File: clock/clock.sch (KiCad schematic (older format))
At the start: 2 parts

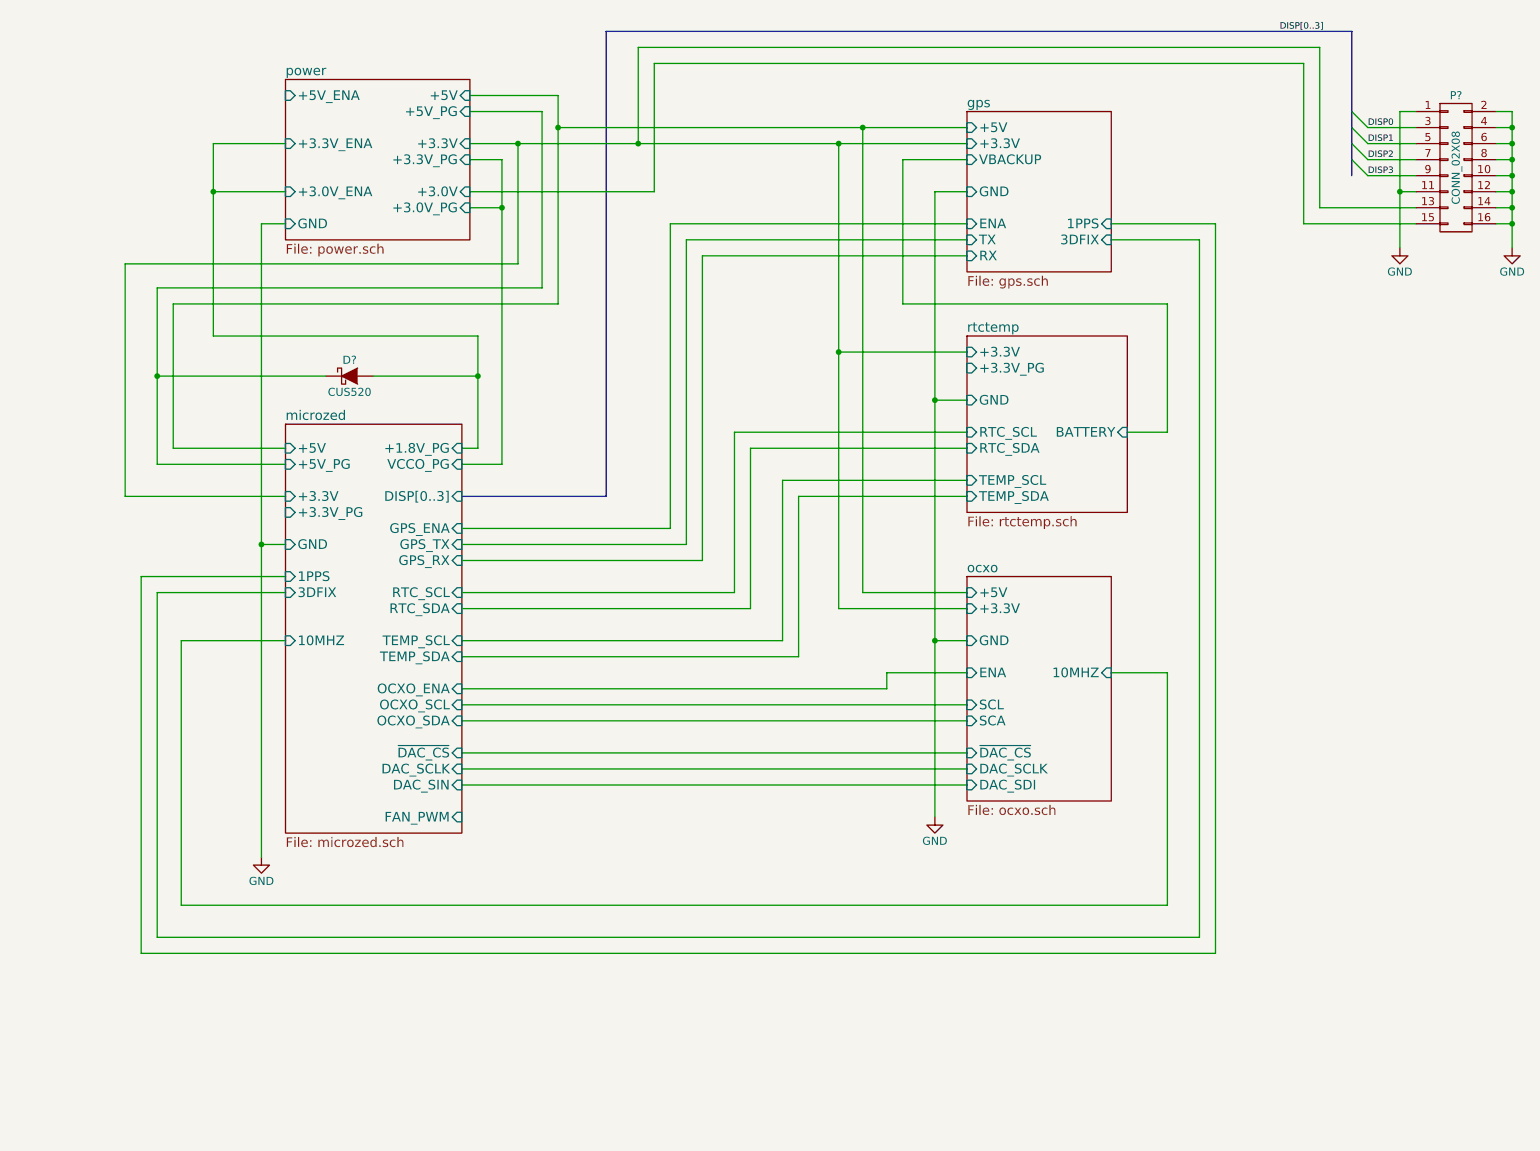
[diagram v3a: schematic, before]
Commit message: Add proper loading and buffer to the OCXO output.
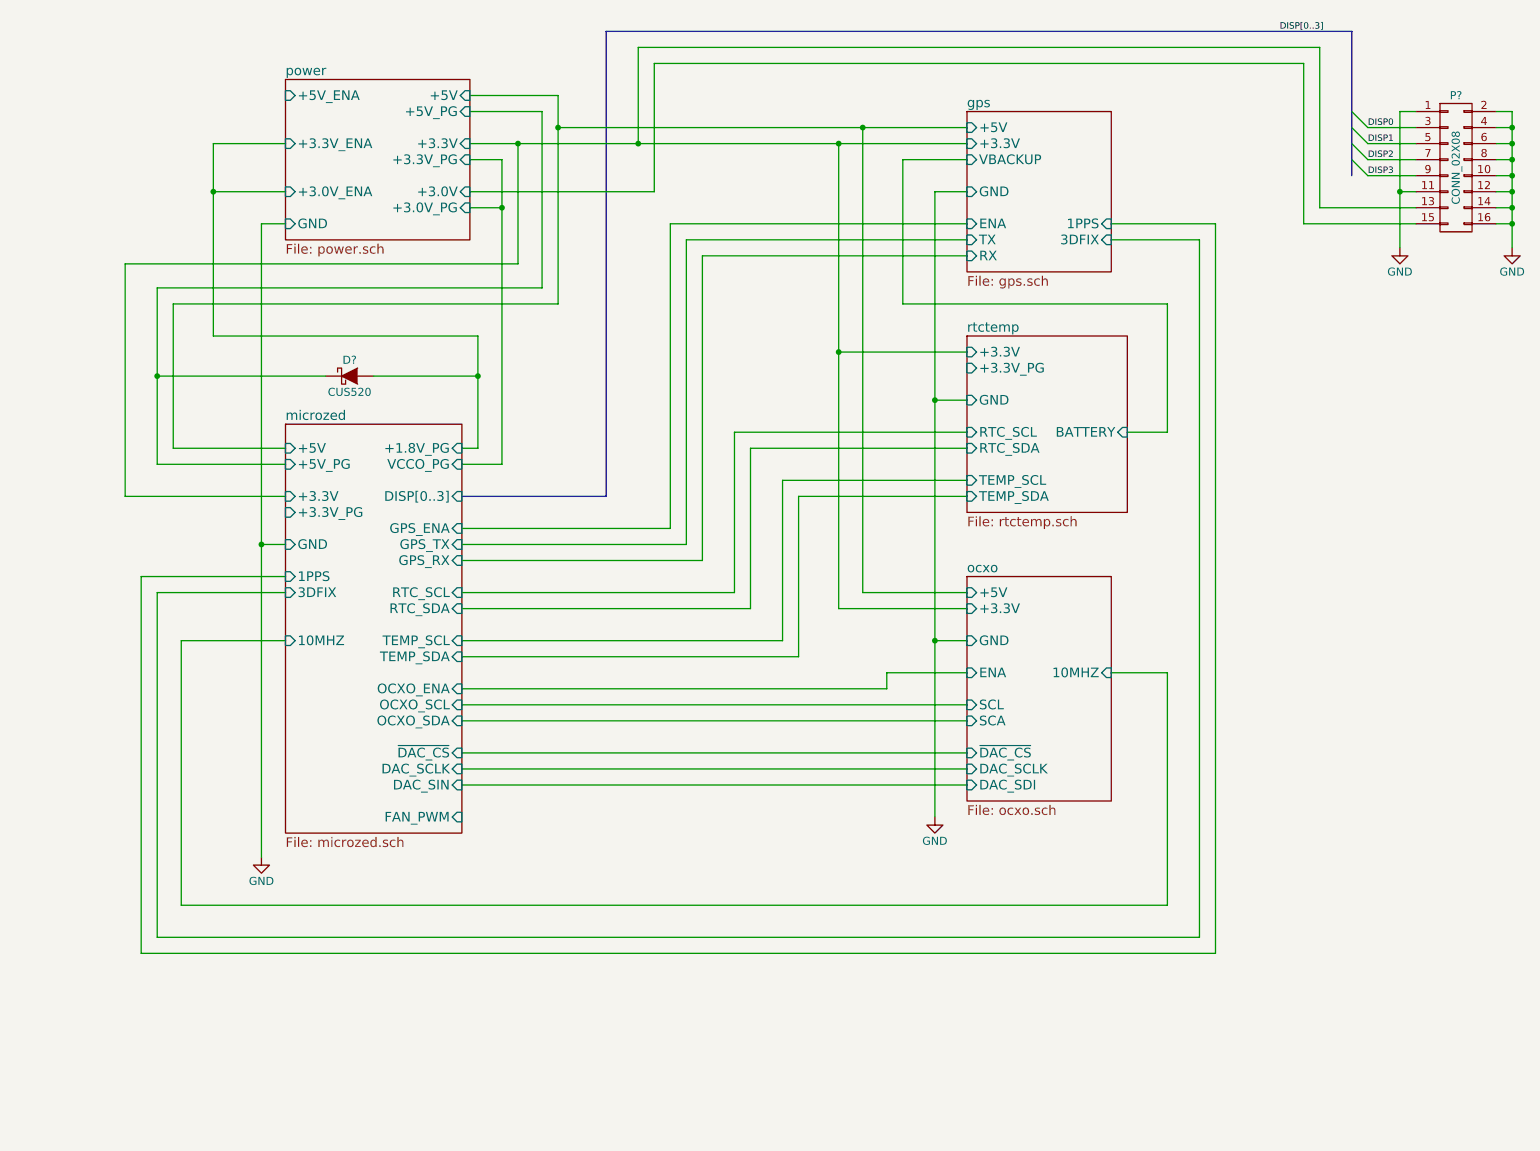
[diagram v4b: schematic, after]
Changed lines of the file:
@@
 	3550 1000 4100 1000
 Wire Wire Line
-	4100 1000 4100 1200
-Wire Wire Line
-	4100 1200 4100 2300
+	4100 1000 4100 2300
 Wire Wire Line
 	4100 2300 1700 2300
@@
 	4000 1100 4000 2200
 Wire Wire Line
-	1950 1300 1950 1600
-Wire Wire Line
-	1950 1600 1950 2500
+	1950 1300 1950 2500
 Wire Wire Line
 	1950 1300 2400 1300
@@
 	1750 4400 2400 4400
 Wire Wire Line
-	4100 1200 6000 1200
-Wire Wire Line
-	6000 1200 6650 1200
-Wire Wire Line
-	3550 1300 3850 1300
-Wire Wire Line
-	3850 1300 4600 1300
-Wire Wire Line
-	4600 1300 5850 1300
-Wire Wire Line
-	5850 1300 6650 1300
+	4100 1200 6650 1200
+Wire Wire Line
+	3550 1300 6650 1300
 Wire Wire Line
 	6000 1200 6000 4100
@@
 	5850 4200 6650 4200
 Wire Wire Line
-	5850 1300 5850 2600
-Wire Wire Line
-	5850 2600 5850 4200
+	5850 1300 5850 4200
 Connection ~ 5850 1300
 Wire Wire Line
@@
 	2400 3800 2250 3800
 Wire Wire Line
-	2250 1800 2250 3800
-Wire Wire Line
-	2250 3800 2250 5750
+	2250 1800 2250 5750
 Wire Wire Line
 	6650 1600 6450 1600
 Wire Wire Line
-	6450 1600 6450 2900
-Wire Wire Line
-	6450 2900 6450 4400
-Wire Wire Line
-	6450 4400 6450 5500
+	6450 1600 6450 5500
 Wire Wire Line
 	2400 1800 2250 1800
@@
 	3550 1400 3750 1400
 Wire Wire Line
-	3750 1400 3750 1700
-Wire Wire Line
-	3750 1700 3750 3300
+	3750 1400 3750 3300
 Wire Wire Line
 	3750 3300 3500 3300
@@
 	3600 3200 3500 3200
 Wire Wire Line
-	3600 2500 3600 2750
-Wire Wire Line
-	3600 2750 3600 3200
+	3600 2500 3600 3200
 Wire Wire Line
 	1950 2500 3600 2500
@@
 	4000 2200 1600 2200
 Wire Wire Line
-	1600 2200 1600 2750
-Wire Wire Line
-	1600 2750 1600 3300
+	1600 2200 1600 3300
 Wire Wire Line
 	1600 3300 2400 3300
@@
 	9950 1100 10050 1100
 Wire Wire Line
-	10050 1100 10050 1200
-Wire Wire Line
-	10050 1200 10050 1300
-Wire Wire Line
-	10050 1300 10050 1400
-Wire Wire Line
-	10050 1400 10050 1500
-Wire Wire Line
-	10050 1500 10050 1600
-Wire Wire Line
-	10050 1600 10050 1700
-Wire Wire Line
-	10050 1700 10050 1800
-Wire Wire Line
-	10050 1800 10050 1950
+	10050 1100 10050 1950
 Wire Wire Line
 	9950 1800 10050 1800
@@
 	9450 1100 9350 1100
 Wire Wire Line
-	9350 1100 9350 1600
-Wire Wire Line
-	9350 1600 9350 1950
+	9350 1100 9350 1950
 Wire Wire Line
 	9450 1600 9350 1600
@@
 	4400 600  9050 600
 Wire Bus Line
-	9050 600  9050 1100
-Wire Bus Line
-	9050 1100 9050 1200
-Wire Bus Line
-	9050 1200 9050 1300
-Wire Bus Line
-	9050 1300 9050 1400
-Wire Bus Line
-	9050 1400 9050 1500
+	9050 600  9050 1500
 Entry Wire Line
 	9050 1100 9150 1200

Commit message: Fan and power connectors.
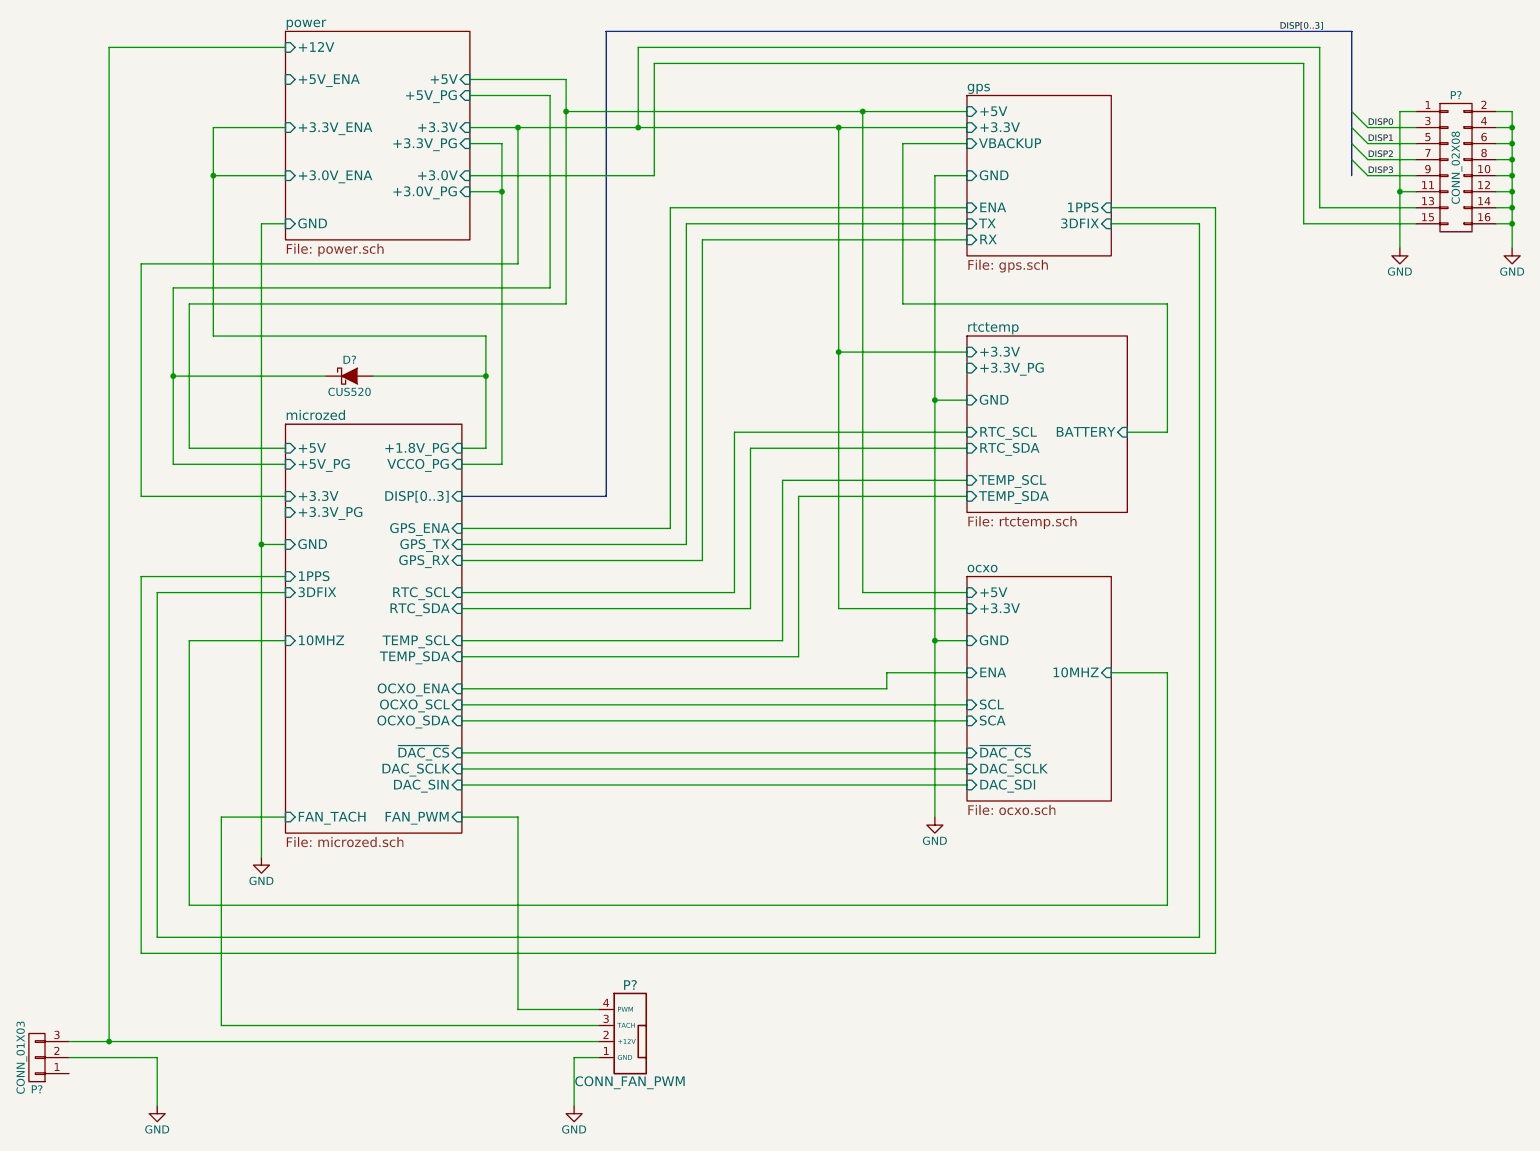
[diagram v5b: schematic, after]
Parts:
- added P?: CONN_01X03, symbol CONN_01X03
- added P?: CONN_FAN_PWM, symbol CONN_FAN_PWM
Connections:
- net GND: now also P?.1 (GND), P?.2 (P2)
- net microzed/FAN_PWM: now also P?.4 (PWM)
- new net microzed/FAN_TACH: P?.3 (TACH)
- new net power/+12V: P?.2 (+12V), P?.3 (P3)
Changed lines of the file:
@@
 $EndSheet
 $Sheet
-S 6650 1100 900  1000
+S 6650 1000 900  1000
 U 56133D72
 F0 "gps" 60
 F1 "gps.sch" 60
-F2 "+5V" I L 6650 1200 60
-F3 "+3.3V" I L 6650 1300 60
-F4 "TX" I L 6650 1900 60
-F5 "RX" I L 6650 2000 60
-F6 "1PPS" I R 7550 1800 60
-F7 "3DFIX" I R 7550 1900 60
-F8 "VBACKUP" I L 6650 1400 60
-F9 "GND" I L 6650 1600 60
-F10 "ENA" I L 6650 1800 60
+F2 "+5V" I L 6650 1100 60
+F3 "+3.3V" I L 6650 1200 60
+F4 "TX" I L 6650 1800 60
+F5 "RX" I L 6650 1900 60
+F6 "1PPS" I R 7550 1700 60
+F7 "3DFIX" I R 7550 1800 60
+F8 "VBACKUP" I L 6650 1300 60
+F9 "GND" I L 6650 1500 60
+F10 "ENA" I L 6650 1700 60
 $EndSheet
 $Sheet
@@
 F25 "TEMP_SCL" I R 3500 4400 60
 F26 "TEMP_SDA" I R 3500 4500 60
+F27 "FAN_TACH" I L 2400 5500 60
 $EndSheet
 Wire Wire Line
-	3550 1000 4100 1000
-Wire Wire Line
-	4100 1000 4100 2300
-Wire Wire Line
-	4100 2300 1700 2300
-Wire Wire Line
-	1700 2300 1700 3200
-Wire Wire Line
-	1700 3200 2400 3200
-Wire Wire Line
-	3550 1100 4000 1100
-Wire Wire Line
-	4000 1100 4000 2200
-Wire Wire Line
-	1950 1300 1950 2500
-Wire Wire Line
-	1950 1300 2400 1300
-Wire Wire Line
-	2400 1600 1950 1600
-Connection ~ 1950 1600
+	3550 900  4150 900
+Wire Wire Line
+	4150 900  4150 2300
+Wire Wire Line
+	4150 2300 1800 2300
+Wire Wire Line
+	1800 2300 1800 3200
+Wire Wire Line
+	1800 3200 2400 3200
+Wire Wire Line
+	3550 1000 4050 1000
+Wire Wire Line
+	4050 1000 4050 2200
+Wire Wire Line
+	1950 1200 1950 2500
+Wire Wire Line
+	1950 1200 2400 1200
+Wire Wire Line
+	2400 1500 1950 1500
+Connection ~ 1950 1500
 Wire Wire Line
 	7550 4600 7900 4600
@@
 	7900 4600 7900 6050
 Wire Wire Line
-	7900 6050 1750 6050
-Wire Wire Line
-	1750 6050 1750 4400
-Wire Wire Line
-	1750 4400 2400 4400
-Wire Wire Line
-	4100 1200 6650 1200
-Wire Wire Line
-	3550 1300 6650 1300
-Wire Wire Line
-	6000 1200 6000 4100
+	7900 6050 1800 6050
+Wire Wire Line
+	1800 6050 1800 4400
+Wire Wire Line
+	1800 4400 2400 4400
+Wire Wire Line
+	4150 1100 6650 1100
+Wire Wire Line
+	3550 1200 6650 1200
+Wire Wire Line
+	6000 1100 6000 4100
 Wire Wire Line
 	6000 4100 6650 4100
-Connection ~ 6000 1200
+Connection ~ 6000 1100
 Wire Wire Line
 	5850 4200 6650 4200
 Wire Wire Line
-	5850 1300 5850 4200
-Connection ~ 5850 1300
+	5850 1200 5850 4200
+Connection ~ 5850 1200
 Wire Wire Line
 	6150 4700 3500 4700
@@
 	3500 3700 4800 3700
 Wire Wire Line
-	4800 3700 4800 1800
-Wire Wire Line
-	4800 1800 6650 1800
-Wire Wire Line
-	6650 1900 4900 1900
-Wire Wire Line
-	4900 1900 4900 3800
+	4800 3700 4800 1700
+Wire Wire Line
+	4800 1700 6650 1700
+Wire Wire Line
+	6650 1800 4900 1800
+Wire Wire Line
+	4900 1800 4900 3800
 Wire Wire Line
 	4900 3800 3500 3800
@@
 	3500 3900 5000 3900
 Wire Wire Line
-	5000 3900 5000 2000
-Wire Wire Line
-	5000 2000 6650 2000
-Wire Wire Line
-	7550 1900 8100 1900
-Wire Wire Line
-	8100 1900 8100 6250
+	5000 3900 5000 1900
+Wire Wire Line
+	5000 1900 6650 1900
+Wire Wire Line
+	7550 1800 8100 1800
+Wire Wire Line
+	8100 1800 8100 6250
 Wire Wire Line
 	8100 6250 1600 6250
@@
 	1500 6350 8200 6350
 Wire Wire Line
-	8200 6350 8200 1800
-Wire Wire Line
-	8200 1800 7550 1800
-Wire Wire Line
-	3850 1300 3850 2050
-Wire Wire Line
-	3850 2050 1400 2050
-Wire Wire Line
-	1400 2050 1400 3500
-Wire Wire Line
-	1400 3500 2400 3500
-Connection ~ 3850 1300
+	8200 6350 8200 1700
+Wire Wire Line
+	8200 1700 7550 1700
+Wire Wire Line
+	3850 1200 3850 2050
+Wire Wire Line
+	3850 2050 1500 2050
+Wire Wire Line
+	1500 2050 1500 3500
+Wire Wire Line
+	1500 3500 2400 3500
+Connection ~ 3850 1200
 Wire Wire Line
 	2400 3800 2250 3800
@@
 	2250 1800 2250 5750
 Wire Wire Line
-	6650 1600 6450 1600
-Wire Wire Line
-	6450 1600 6450 5500
+	6650 1500 6450 1500
+Wire Wire Line
+	6450 1500 6450 5500
 Wire Wire Line
 	2400 1800 2250 1800
@@
 $EndComp
 Wire Wire Line
-	3550 1400 3750 1400
-Wire Wire Line
-	3750 1400 3750 3300
+	3550 1300 3750 1300
+Wire Wire Line
+	3750 1300 3750 3300
 Wire Wire Line
 	3750 3300 3500 3300
 Wire Wire Line
-	3750 1700 3550 1700
-Connection ~ 3750 1700
-Wire Wire Line
-	3600 3200 3500 3200
-Wire Wire Line
-	3600 2500 3600 3200
-Wire Wire Line
-	1950 2500 3600 2500
-Wire Wire Line
-	4000 2200 1600 2200
-Wire Wire Line
-	1600 2200 1600 3300
-Wire Wire Line
-	1600 3300 2400 3300
+	3750 1600 3550 1600
+Connection ~ 3750 1600
+Wire Wire Line
+	3650 3200 3500 3200
+Wire Wire Line
+	3650 2500 3650 3200
+Wire Wire Line
+	1950 2500 3650 2500
+Wire Wire Line
+	4050 2200 1700 2200
+Wire Wire Line
+	1700 2200 1700 3300
+Wire Wire Line
+	1700 3300 2400 3300
 $Comp
 L D_Schottky D?
@@
 $EndComp
 Wire Wire Line
-	3600 2750 2950 2750
-Connection ~ 3600 2750
-Wire Wire Line
-	2650 2750 1600 2750
-Connection ~ 1600 2750
+	3650 2750 2950 2750
+Connection ~ 3650 2750
+Wire Wire Line
+	2650 2750 1700 2750
+Connection ~ 1700 2750
 $Sheet
-S 2400 900  1150 1000
+S 2400 600  1150 1300
 U 55FF5A67
 F0 "power" 60
 F1 "power.sch" 60
-F2 "+5V" I R 3550 1000 60
-F3 "+3.3V" I R 3550 1300 60
-F4 "+3.0V" I R 3550 1600 60
-F5 "+3.0V_PG" I R 3550 1700 60
-F6 "+3.3V_PG" I R 3550 1400 60
-F7 "+5V_PG" I R 3550 1100 60
-F8 "+5V_ENA" I L 2400 1000 60
-F9 "+3.3V_ENA" I L 2400 1300 60
-F10 "+3.0V_ENA" I L 2400 1600 60
+F2 "+5V" I R 3550 900 60
+F3 "+3.3V" I R 3550 1200 60
+F4 "+3.0V" I R 3550 1500 60
+F5 "+3.0V_PG" I R 3550 1600 60
+F6 "+3.3V_PG" I R 3550 1300 60
+F7 "+5V_PG" I R 3550 1000 60
+F8 "+5V_ENA" I L 2400 900 60
+F9 "+3.3V_ENA" I L 2400 1200 60
+F10 "+3.0V_ENA" I L 2400 1500 60
 F11 "GND" I L 2400 1800 60
+F12 "+12V" I L 2400 700 60
 $EndSheet
 $Comp
@@
 Connection ~ 9350 1600
 Wire Wire Line
-	3550 1600 4700 1600
-Wire Wire Line
-	4700 1600 4700 800
+	3550 1500 4700 1500
+Wire Wire Line
+	4700 1500 4700 800
 Wire Wire Line
 	4700 800  8750 800
@@
 	8850 700  4600 700
 Wire Wire Line
-	4600 700  4600 1300
-Connection ~ 4600 1300
+	4600 700  4600 1200
+Connection ~ 4600 1200
 $Sheet
 S 6650 2500 1000 1100
@@
 	7900 2300 6250 2300
 Wire Wire Line
-	6250 2300 6250 1400
-Wire Wire Line
-	6250 1400 6650 1400
+	6250 2300 6250 1300
+Wire Wire Line
+	6250 1300 6650 1300
 Wire Bus Line
 	3500 3500 4400 3500
@@
 Wire Wire Line
 	6150 4600 6150 4700
-Connection ~ 4100 1200
+Connection ~ 4150 1100
+$Comp
+L CONN_FAN_PWM P?
+U 1 1 563D6A73
+P 4550 6850
+F 0 "P?" H 4550 7150 60  0000 C CNN
+F 1 "CONN_FAN_PWM" H 4550 6550 60  0000 C CNN
+F 2 "" H 4750 6800 60  0000 C CNN
+F 3 "" H 4750 6800 60  0000 C CNN
+F 4 "Molex" H 4550 7350 50  0001 C CNN "Manufacturer"
+F 5 "47053-1000" H 4550 7250 50  0001 C CNN "PartNum"
+	1    4550 6850
+	1    0    0    -1
+$EndComp
+Wire Wire Line
+	3500 5500 3850 5500
+Wire Wire Line
+	3850 5500 3850 6700
+Wire Wire Line
+	3850 6700 4350 6700
+Wire Wire Line
+	2000 6800 4350 6800
+Wire Wire Line
+	2000 6800 2000 5500
+Wire Wire Line
+	2000 5500 2400 5500
+$Comp
+L GND #PWR?
+U 1 1 563D71E9
+P 4200 7300
+F 0 "#PWR?" H 4200 7050 50  0001 C CNN
+F 1 "GND" H 4200 7150 50  0000 C CNN
+F 2 "" H 4200 7300 60  0000 C CNN
+F 3 "" H 4200 7300 60  0000 C CNN
+	1    4200 7300
+	1    0    0    -1
+$EndComp
+Wire Wire Line
+	4350 7000 4200 7000
+Wire Wire Line
+	4200 7000 4200 7300
+Wire Wire Line
+	2400 700  1300 700
+Wire Wire Line
+	1300 700  1300 6900
+Wire Wire Line
+	1050 6900 4350 6900
+$Comp
+L CONN_01X03 P?
+U 1 1 563D5B9B
+P 850 7000
+F 0 "P?" H 850 7200 50  0000 C CNN
+F 1 "CONN_01X03" V 950 7000 50  0000 C CNN
+F 2 "" H 850 7000 60  0000 C CNN
+F 3 "" H 850 7000 60  0000 C CNN
+	1    850  7000
+	-1   0    0    1
+$EndComp
+Connection ~ 1300 6900
+Wire Wire Line
+	1050 7000 1600 7000
+Wire Wire Line
+	1600 7000 1600 7300
+$Comp
+L GND #PWR?
+U 1 1 563D694B
+P 1600 7300
+F 0 "#PWR?" H 1600 7050 50  0001 C CNN
+F 1 "GND" H 1600 7150 50  0000 C CNN
+F 2 "" H 1600 7300 60  0000 C CNN
+F 3 "" H 1600 7300 60  0000 C CNN
+	1    1600 7300
+	1    0    0    -1
+$EndComp
 $EndSCHEMATC
